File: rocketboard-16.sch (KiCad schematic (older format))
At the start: 113 parts, among them J1 SWD, K1 MX_RGB, K10 MX_RGB, K11 MX_RGB, K12 MX_RGB, K13 MX_RGB, K14 MX_RGB, K15 MX_RGB, K16 MX_RGB, K2 MX_RGB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

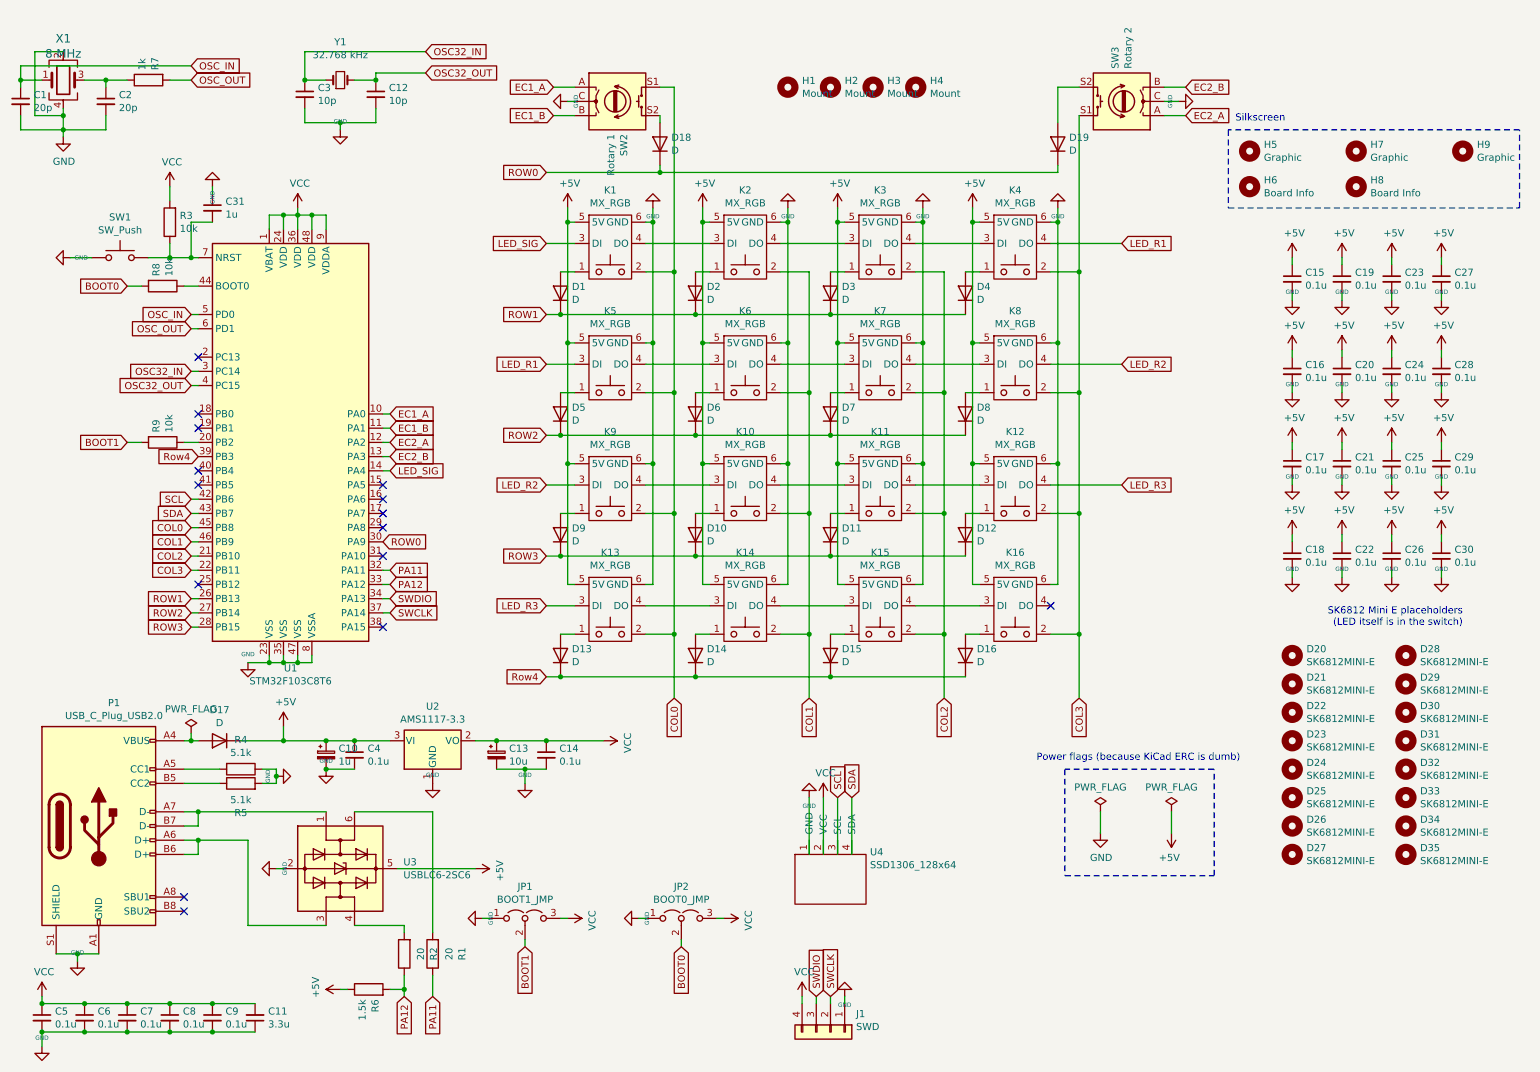
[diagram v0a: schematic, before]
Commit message: Needed to add debounce and pullups to the rotary encoder lines, added to sch and updated PCB
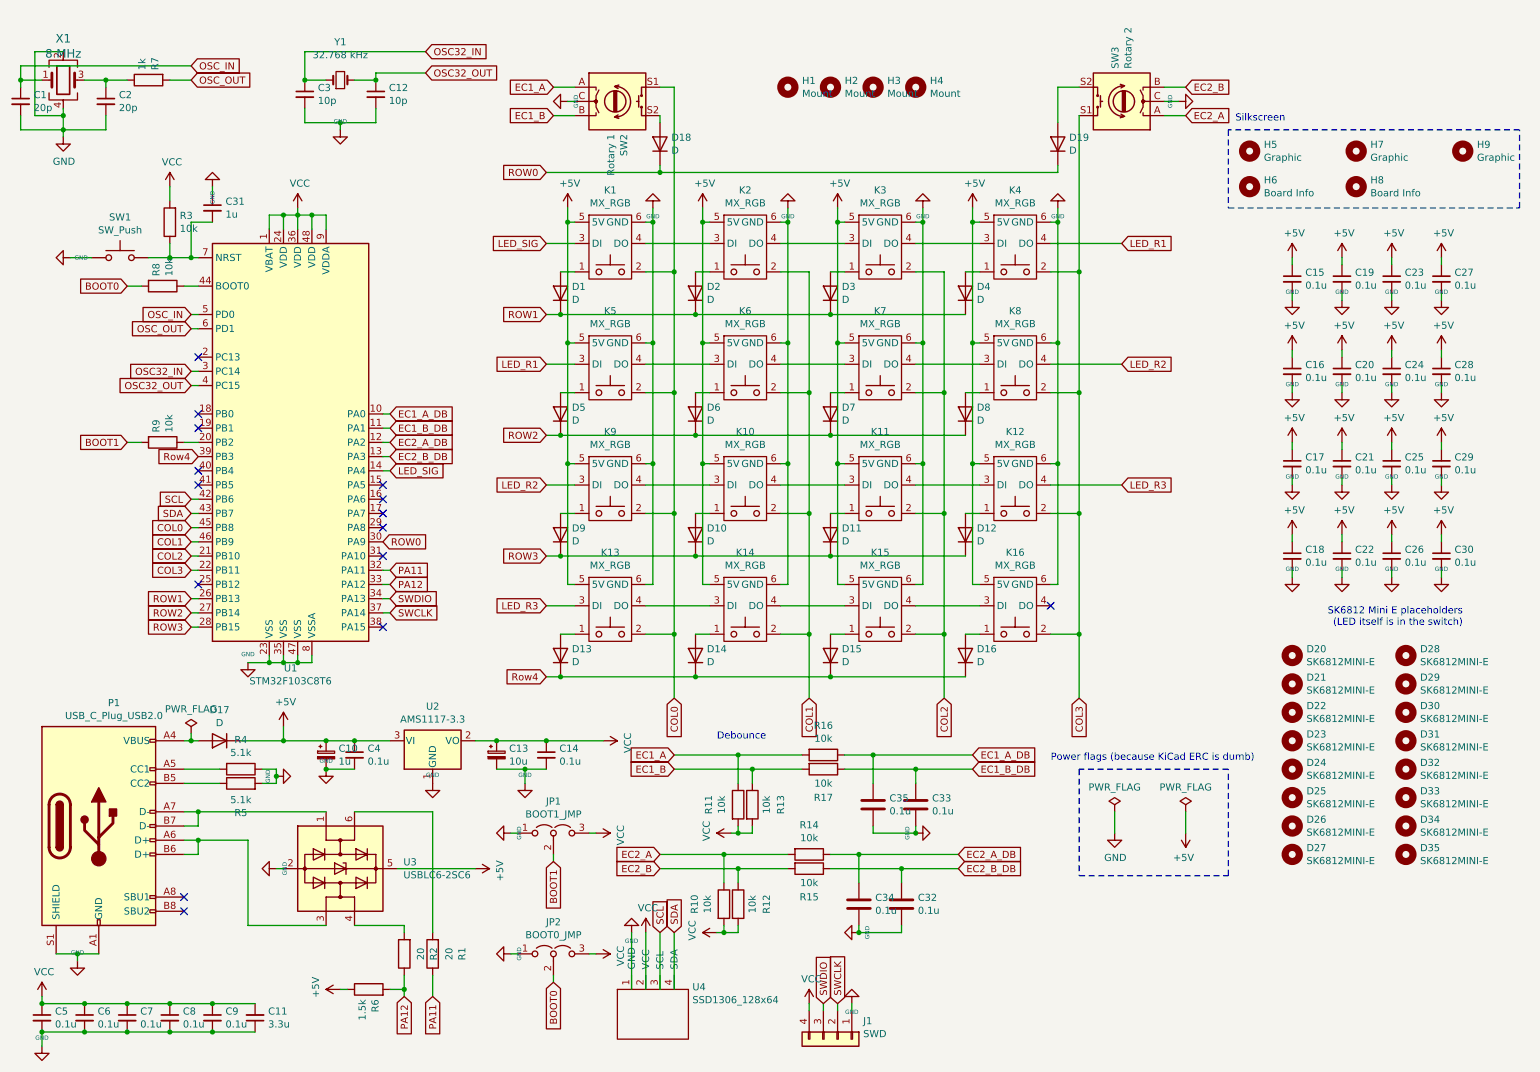
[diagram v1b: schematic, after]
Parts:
- added C32, C33, C34, C35: 0.1u, Capacitor_SMD:C_0603_1608Metric, symbol Device:C
- added R10, R11, R12, R13, R14, R15, R16, R17: 10k, Resistor_SMD:R_0603_1608Metric, symbol Device:R
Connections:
- net EC1_A: now also R11.1, R16.2; no longer U1.10 (PA0)
- net EC1_B: now also R13.1, R17.2; no longer U1.11 (PA1)
- net EC2_A: now also R10.1, R14.2; no longer U1.12 (PA2)
- net EC2_B: now also R12.1, R15.2; no longer U1.13 (PA3)
- net GND: now also C32.2, C33.2, C34.2, C35.2
- net VCC: now also R10.2, R11.2, R12.2, R13.2
- new net EC1_A_DB: C35.1, R16.1, U1.10 (PA0)
- new net EC1_B_DB: C33.1, R17.1, U1.11 (PA1)
- new net EC2_A_DB: C34.1, R14.1, U1.12 (PA2)
- new net EC2_B_DB: C32.1, R15.1, U1.13 (PA3)
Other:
- note added: "Debounce"
- moved on the sheet: J1, JP1, JP2, U4

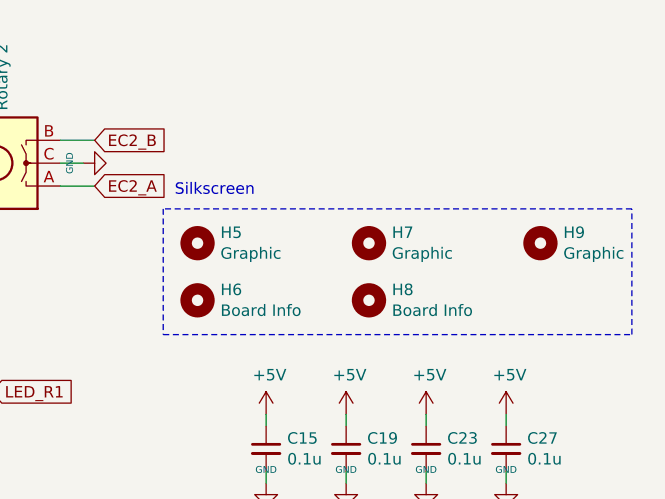
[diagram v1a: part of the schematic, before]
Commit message: Added hubble, iss, and spacewalk graphics to sch/pcb
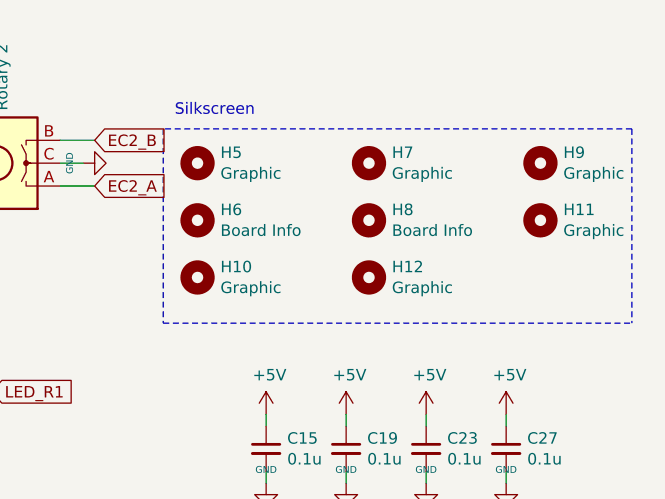
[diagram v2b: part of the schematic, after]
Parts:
- added H10: Graphic, seth-logo:iss, symbol Mechanical:MountingHole
- added H11: Graphic, seth-logo:spacewalk, symbol Mechanical:MountingHole
- added H12: Graphic, seth-logo:hubble_space_telescope, symbol Mechanical:MountingHole
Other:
- moved on the sheet: H5, H6, H7, H8, H9
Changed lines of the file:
@@
 L Mechanical:MountingHole H5
 U 1 1 5FDE416C
-P 9250 1350
-F 0 "H5" H 9350 1396 50  0000 L CNN
-F 1 "Graphic" H 9350 1305 50  0000 L CNN
-F 2 "seth-logo:saturn_v_simplified" H 9250 1350 50  0001 C CNN
-F 3 "~" H 9250 1350 50  0001 C CNN
-	1    9250 1350
+P 9250 1000
+F 0 "H5" H 9350 1046 50  0000 L CNN
+F 1 "Graphic" H 9350 955 50  0000 L CNN
+F 2 "seth-logo:saturn_v_simplified" H 9250 1000 50  0001 C CNN
+F 3 "~" H 9250 1000 50  0001 C CNN
+	1    9250 1000
 	1    0    0    -1
 $EndComp
@@
 L Mechanical:MountingHole H7
 U 1 1 5FF060AE
-P 10000 1350
-F 0 "H7" H 10100 1396 50  0000 L CNN
-F 1 "Graphic" H 10100 1305 50  0000 L CNN
-F 2 "seth-logo:lunar_module" H 10000 1350 50  0001 C CNN
-F 3 "~" H 10000 1350 50  0001 C CNN
-	1    10000 1350
+P 10000 1000
+F 0 "H7" H 10100 1046 50  0000 L CNN
+F 1 "Graphic" H 10100 955 50  0000 L CNN
+F 2 "seth-logo:lunar_module" H 10000 1000 50  0001 C CNN
+F 3 "~" H 10000 1000 50  0001 C CNN
+	1    10000 1000
 	1    0    0    -1
 $EndComp
@@
 L Mechanical:MountingHole H9
 U 1 1 5FF24C73
-P 10750 1350
-F 0 "H9" H 10850 1396 50  0000 L CNN
-F 1 "Graphic" H 10850 1305 50  0000 L CNN
-F 2 "seth-logo:space_shuttle" H 10750 1350 50  0001 C CNN
-F 3 "~" H 10750 1350 50  0001 C CNN
-	1    10750 1350
+P 10750 1000
+F 0 "H9" H 10850 1046 50  0000 L CNN
+F 1 "Graphic" H 10850 955 50  0000 L CNN
+F 2 "seth-logo:space_shuttle" H 10750 1000 50  0001 C CNN
+F 3 "~" H 10750 1000 50  0001 C CNN
+	1    10750 1000
 	1    0    0    -1
 $EndComp
@@
 L Mechanical:MountingHole H6
 U 1 1 5FF438B1
-P 9250 1600
-F 0 "H6" V 9204 1700 50  0000 L CNN
-F 1 "Board Info" V 9295 1700 50  0000 L CNN
-F 2 "seth-logo:board-title" H 9250 1600 50  0001 C CNN
-F 3 "~" H 9250 1600 50  0001 C CNN
-	1    9250 1600
+P 9250 1250
+F 0 "H6" V 9204 1350 50  0000 L CNN
+F 1 "Board Info" V 9295 1350 50  0000 L CNN
+F 2 "seth-logo:board-title" H 9250 1250 50  0001 C CNN
+F 3 "~" H 9250 1250 50  0001 C CNN
+	1    9250 1250
 	0    1    1    0
 $EndComp
@@
 L Mechanical:MountingHole H8
 U 1 1 6001AA81
-P 10000 1600
-F 0 "H8" V 9954 1700 50  0000 L CNN
-F 1 "Board Info" V 10045 1700 50  0000 L CNN
-F 2 "seth-logo:text" H 10000 1600 50  0001 C CNN
-F 3 "~" H 10000 1600 50  0001 C CNN
-	1    10000 1600
+P 10000 1250
+F 0 "H8" V 9954 1350 50  0000 L CNN
+F 1 "Board Info" V 10045 1350 50  0000 L CNN
+F 2 "seth-logo:text" H 10000 1250 50  0001 C CNN
+F 3 "~" H 10000 1250 50  0001 C CNN
+	1    10000 1250
 	0    1    1    0
 $EndComp
 Wire Notes Line
-	9100 1200 9100 1750
+	9100 1700 11150 1700
 Wire Notes Line
-	9100 1750 11150 1750
-Wire Notes Line
-	11150 1750 11150 1200
-Wire Notes Line
-	11150 1200 9100 1200
-Text Notes 9150 1150 0    50   ~ 0
+	11150 850  9100 850
+Text Notes 9150 800  0    50   ~ 0
 Silkscreen
 Text GLabel 5200 5600 0    50   Input ~ 0
@@
 Text GLabel 3200 3200 2    50   Input ~ 0
 EC1_A_DB
+$Comp
+L Mechanical:MountingHole H11
+U 1 1 5F6BC792
+P 10750 1250
+F 0 "H11" H 10850 1296 50  0000 L CNN
+F 1 "Graphic" H 10850 1205 50  0000 L CNN
+F 2 "seth-logo:spacewalk" H 10750 1250 50  0001 C CNN
+F 3 "~" H 10750 1250 50  0001 C CNN
+	1    10750 1250
+	1    0    0    -1
+$EndComp
+$Comp
+L Mechanical:MountingHole H10
+U 1 1 5F77B490
+P 9250 1500
+F 0 "H10" H 9350 1546 50  0000 L CNN
+F 1 "Graphic" H 9350 1455 50  0000 L CNN
+F 2 "seth-logo:iss" H 9250 1500 50  0001 C CNN
+F 3 "~" H 9250 1500 50  0001 C CNN
+	1    9250 1500
+	1    0    0    -1
+$EndComp
+Wire Notes Line
+	11150 850  11150 1700
+Wire Notes Line
+	9100 850  9100 1700
+$Comp
+L Mechanical:MountingHole H12
+U 1 1 5F87CD7E
+P 10000 1500
+F 0 "H12" H 10100 1546 50  0000 L CNN
+F 1 "Graphic" H 10100 1455 50  0000 L CNN
+F 2 "seth-logo:hubble_space_telescope" H 10000 1500 50  0001 C CNN
+F 3 "~" H 10000 1500 50  0001 C CNN
+	1    10000 1500
+	1    0    0    -1
+$EndComp
 $EndSCHEMATC

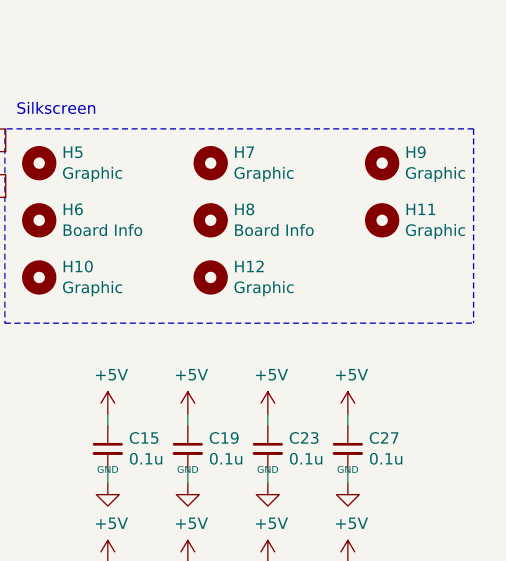
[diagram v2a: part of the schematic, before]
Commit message: Added JLC text for JLC's part number to the schematic
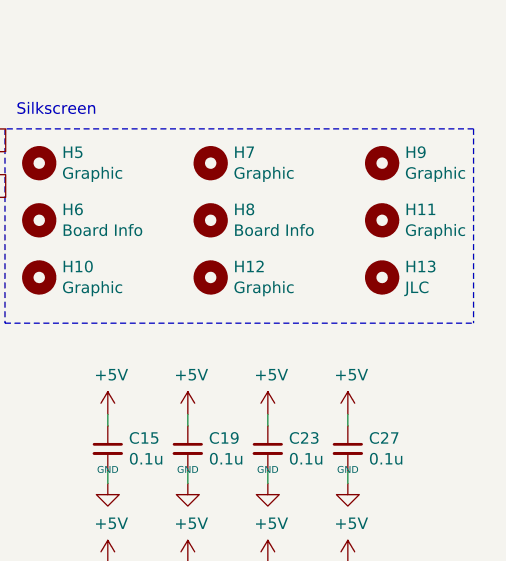
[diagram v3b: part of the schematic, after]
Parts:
- added H13: JLC, seth-logo:text, symbol Mechanical:MountingHole
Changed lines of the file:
@@
+	1    0    0    -1
+$EndComp
+$Comp
+L Mechanical:MountingHole H13
+U 1 1 5F881D48
+P 10750 1500
+F 0 "H13" H 10850 1546 50  0000 L CNN
+F 1 "JLC" H 10850 1455 50  0000 L CNN
+F 2 "seth-logo:text" H 10750 1500 50  0001 C CNN
+F 3 "~" H 10750 1500 50  0001 C CNN
+	1    10750 1500
 	1    0    0    -1
 $EndComp

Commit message: Removed JLC text (will pay the $1.50 to not have it on board)
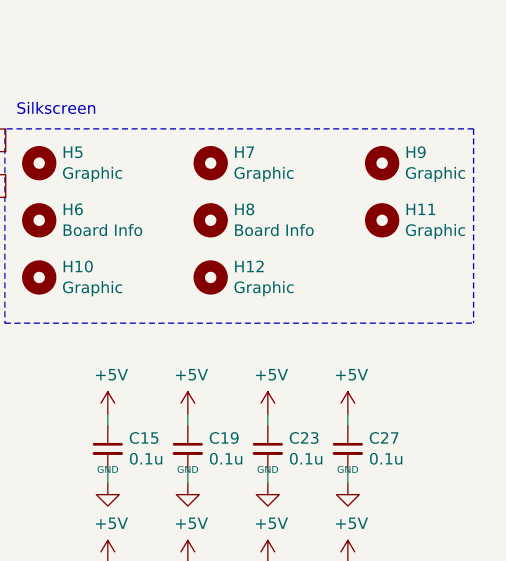
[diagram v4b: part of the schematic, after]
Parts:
- removed H13: JLC, seth-logo:text, symbol Mechanical:MountingHole
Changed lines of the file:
@@
-	1    0    0    -1
-$EndComp
-$Comp
-L Mechanical:MountingHole H13
-U 1 1 5F881D48
-P 10750 1500
-F 0 "H13" H 10850 1546 50  0000 L CNN
-F 1 "JLC" H 10850 1455 50  0000 L CNN
-F 2 "seth-logo:text" H 10750 1500 50  0001 C CNN
-F 3 "~" H 10750 1500 50  0001 C CNN
-	1    10750 1500
 	1    0    0    -1
 $EndComp

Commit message: Updated the USB-C footprint to match the LCSC USB-C connector that works best (>1mm mounting pins)
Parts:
- P1: footprint seth-connectors:USB_C_U262-161N-4BVC11 -> Connector_USB:USB_C_Receptacle_Palconn_UTC16-G
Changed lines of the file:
@@
 F 0 "P1" H 1257 6967 50  0000 C CNN
 F 1 "USB_C_Plug_USB2.0" H 1257 6876 50  0000 C CNN
-F 2 "seth-connectors:USB_C_U262-161N-4BVC11" H 1300 6100 50  0001 C CNN
+F 2 "Connector_USB:USB_C_Receptacle_Palconn_UTC16-G" H 1300 6100 50  0001 C CNN
 F 3 "https://www.usb.org/sites/default/files/documents/usb_type-c.zip" H 1300 6100 50  0001 C CNN
 	1    1150 6100
